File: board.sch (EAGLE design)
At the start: 32 parts, among them IC1 7805T, J1 350428-1

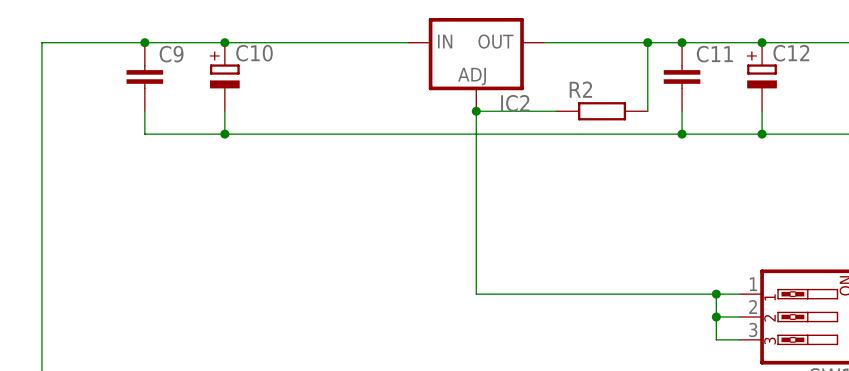
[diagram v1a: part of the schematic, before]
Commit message: Reposicionando na board
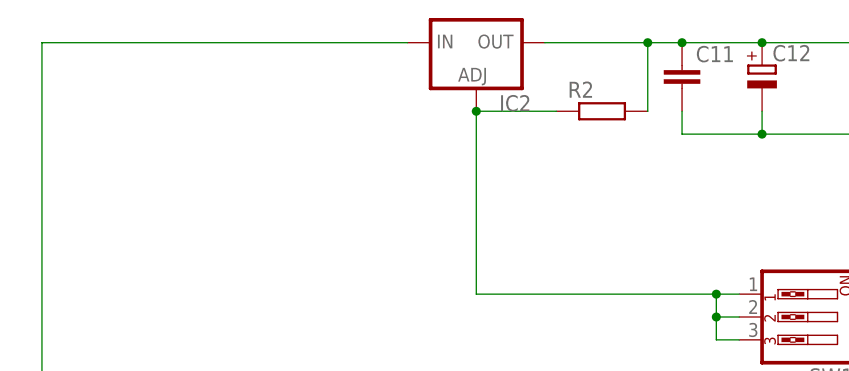
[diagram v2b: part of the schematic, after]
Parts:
- removed C10: (no value), rcl:CPOL-EUE2,5-6E
- removed C9: (no value), rcl:C-EU025-025X050
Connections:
- net GND: no longer C10.-, C9.2
- net N$10: no longer C10.+, C9.1
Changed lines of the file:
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@@
 <part name="C8" library="rcl" library_urn="urn:adsk.eagle:library:334" deviceset="CPOL-EU" device="E2,5-6E" package3d_urn="urn:adsk.eagle:package:23430/1"/>
 <part name="IC2" library="v-reg" library_urn="urn:adsk.eagle:library:409" deviceset="LM317TL" device="" package3d_urn="urn:adsk.eagle:package:30344/1"/>
-<part name="C9" library="rcl" library_urn="urn:adsk.eagle:library:334" deviceset="C-EU" device="025-025X050" package3d_urn="urn:adsk.eagle:package:23629/2"/>
-<part name="C10" library="rcl" library_urn="urn:adsk.eagle:library:334" deviceset="CPOL-EU" device="E2,5-6E" package3d_urn="urn:adsk.eagle:package:23430/1"/>
 <part name="C11" library="rcl" library_urn="urn:adsk.eagle:library:334" deviceset="C-EU" device="025-025X050" package3d_urn="urn:adsk.eagle:package:23629/2"/>
 <part name="C12" library="rcl" library_urn="urn:adsk.eagle:library:334" deviceset="CPOL-EU" device="E2,5-6E" package3d_urn="urn:adsk.eagle:package:23430/1"/>
@@
 <attribute name="NAME" x="69.85" y="161.29" size="1.778" layer="95"/>
 <attribute name="VALUE" x="69.85" y="158.75" size="1.778" layer="96"/>
-</instance>
-<instance part="C9" gate="G$1" x="30.48" y="166.37" smashed="yes">
-<attribute name="NAME" x="32.004" y="166.751" size="1.778" layer="95"/>
-<attribute name="VALUE" x="32.004" y="161.671" size="1.778" layer="96"/>
-</instance>
-<instance part="C10" gate="G$1" x="39.37" y="166.37" smashed="yes">
-<attribute name="NAME" x="40.513" y="166.8526" size="1.778" layer="95"/>
-<attribute name="VALUE" x="40.513" y="161.7726" size="1.778" layer="96"/>
 </instance>
 <instance part="C11" gate="G$1" x="90.17" y="166.37" smashed="yes">
@@
 <pinref part="+12" gate="-2" pin="KL"/>
 <wire x1="95.25" y1="80.01" x2="95.25" y2="82.55" width="0.1524" layer="91"/>
-<pinref part="C10" gate="G$1" pin="-"/>
 <pinref part="C11" gate="G$1" pin="2"/>
 <wire x1="90.17" y1="161.29" x2="90.17" y2="158.75" width="0.1524" layer="91"/>
-<wire x1="90.17" y1="158.75" x2="39.37" y2="158.75" width="0.1524" layer="91"/>
-<wire x1="39.37" y1="158.75" x2="39.37" y2="161.29" width="0.1524" layer="91"/>
-<junction x="39.37" y="158.75"/>
-<pinref part="C9" gate="G$1" pin="2"/>
-<wire x1="30.48" y1="161.29" x2="30.48" y2="158.75" width="0.1524" layer="91"/>
-<wire x1="30.48" y1="158.75" x2="39.37" y2="158.75" width="0.1524" layer="91"/>
 <pinref part="ADJ" gate="-2" pin="KL"/>
 <wire x1="134.62" y1="161.29" x2="134.62" y2="158.75" width="0.1524" layer="91"/>
 <wire x1="90.17" y1="158.75" x2="99.06" y2="158.75" width="0.1524" layer="91"/>
-<junction x="90.17" y="158.75"/>
 <pinref part="C12" gate="G$1" pin="-"/>
 <wire x1="99.06" y1="158.75" x2="129.54" y2="158.75" width="0.1524" layer="91"/>
@@
 <net name="N$10" class="1">
 <segment>
-<wire x1="19.05" y1="168.91" x2="30.48" y2="168.91" width="0.1524" layer="91"/>
-<pinref part="C10" gate="G$1" pin="+"/>
-<wire x1="30.48" y1="168.91" x2="39.37" y2="168.91" width="0.1524" layer="91"/>
-<junction x="39.37" y="168.91"/>
-<pinref part="C9" gate="G$1" pin="1"/>
-<junction x="30.48" y="168.91"/>
 <pinref part="IC2" gate="A" pin="IN"/>
-<wire x1="39.37" y1="168.91" x2="59.69" y2="168.91" width="0.1524" layer="91"/>
+<wire x1="19.05" y1="168.91" x2="59.69" y2="168.91" width="0.1524" layer="91"/>
 <pinref part="D1" gate="1" pin="C"/>
 <pinref part="D2" gate="1" pin="C"/>
